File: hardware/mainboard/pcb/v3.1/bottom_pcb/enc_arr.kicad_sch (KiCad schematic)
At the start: 24 parts

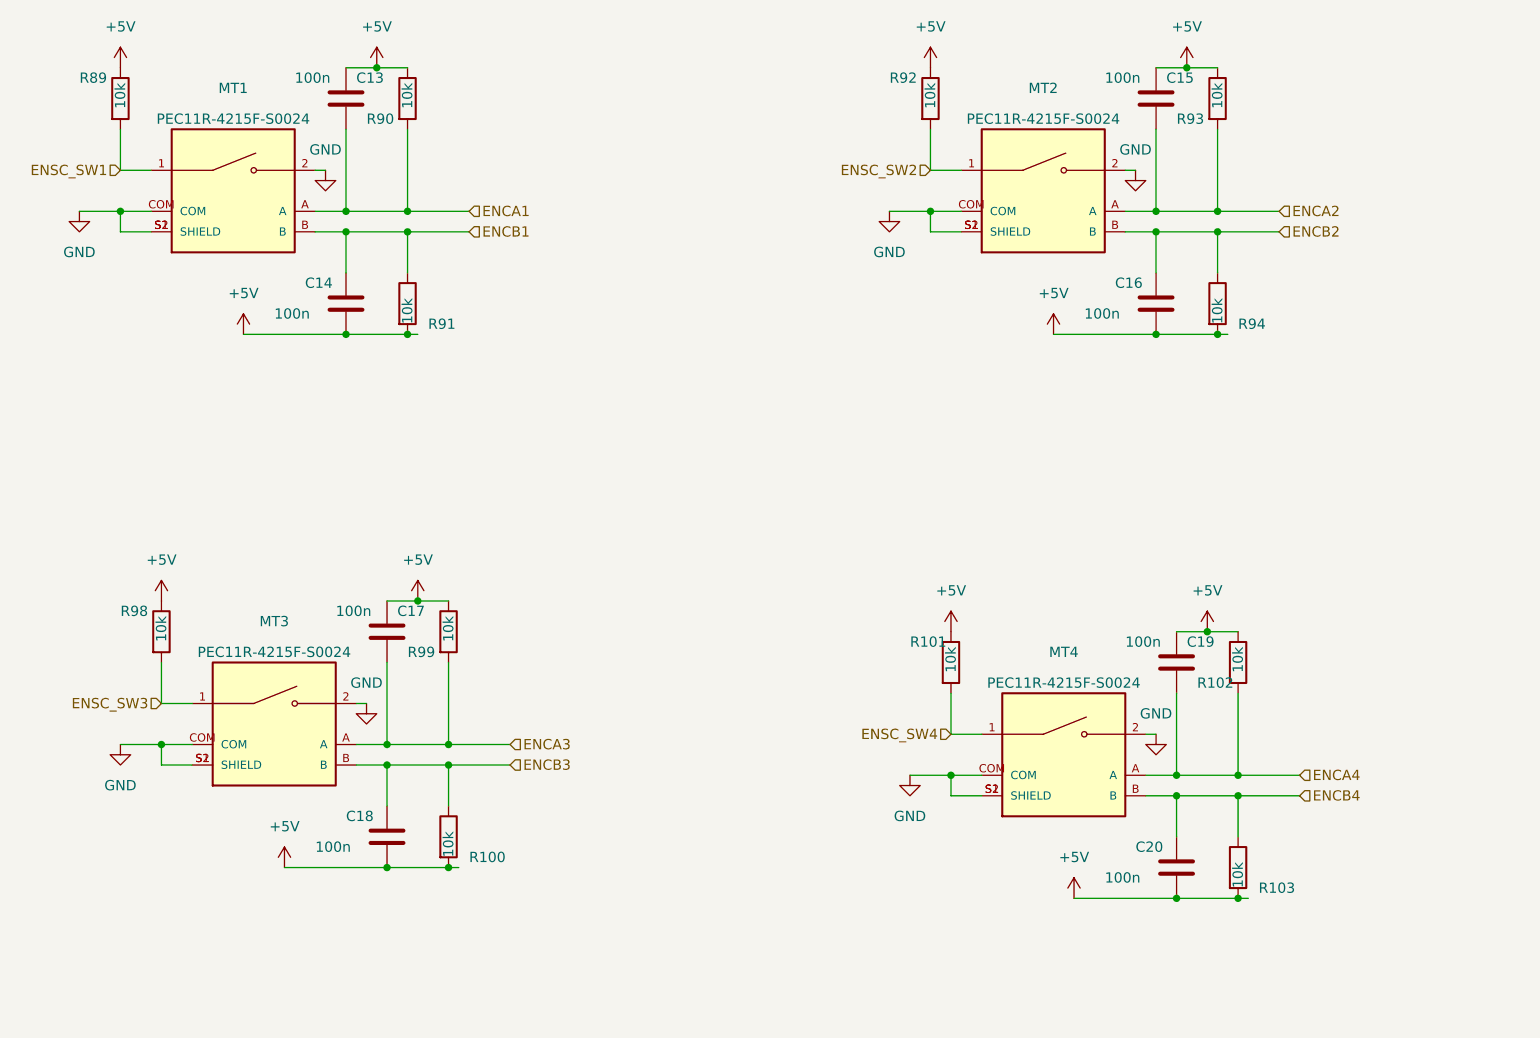
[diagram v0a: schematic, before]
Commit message: pcb cut off
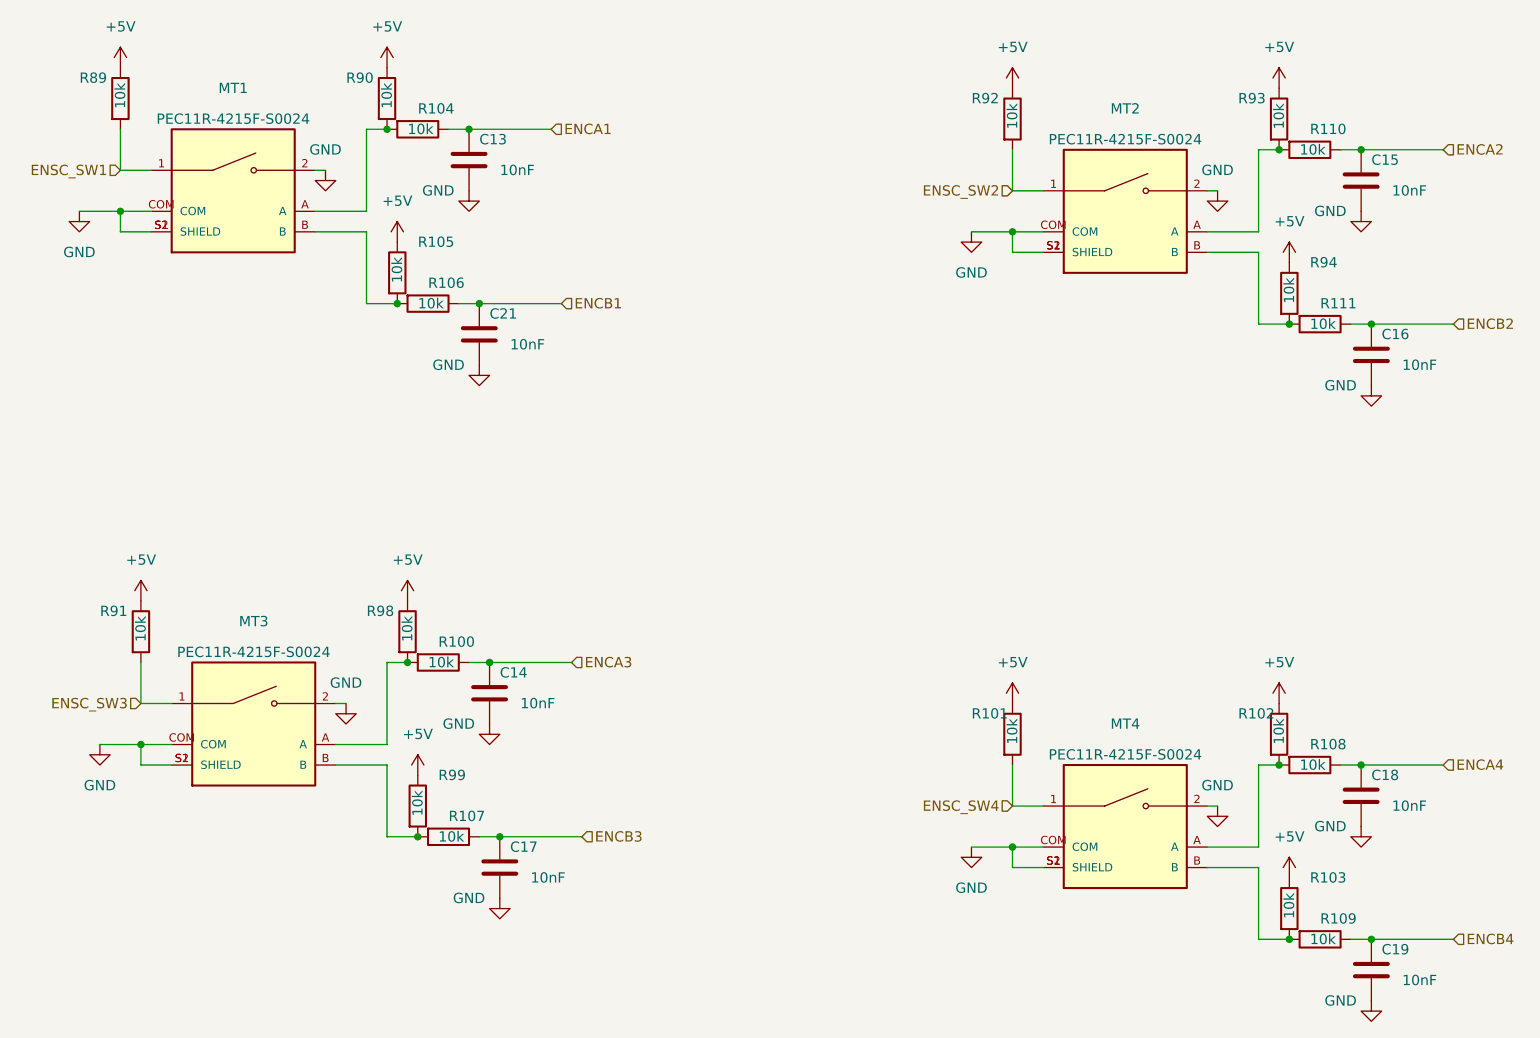
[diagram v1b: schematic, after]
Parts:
- removed C20: 100n, Capacitor_SMD:C_1206_3216Metric_Pad1.33x1.80mm_HandSolder, symbol Device:C
- added C21: 10nF, Capacitor_SMD:C_1206_3216Metric_Pad1.33x1.80mm_HandSolder, symbol Device:C
- added R104, R105, R106, R107, R108, R109, R110, R111: 10k, Resistor_SMD:R_1206_3216Metric_Pad1.30x1.75mm_HandSolder, symbol Device:R
- C13, C14, C15, C16, C17, C18, C19: value 100n -> 10nF
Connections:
- net +5V: now also R103.1, R91.1, R94.1, R105.1; no longer C13.1, C14.2, C15.1, C16.2, C17.1, C18.2, C19.1, R100.2, R103.2, R91.2, R94.2
- net ENCA1: now also C13.1, R104.1; no longer C13.2, MT1.A, R90.2
- net ENCA2: now also C15.1, R110.1; no longer C15.2, MT2.A, R93.2
- net ENCA3: now also C14.1, R100.1; no longer C17.2, MT3.A, R99.2
- net ENCA4: now also C18.1, R108.1; no longer C19.2, MT4.A, R102.2
- net ENCB1: now also C21.1, R106.1; no longer C14.1, MT1.B, R91.1
- net ENCB2: now also R111.1; no longer MT2.B, R94.1
- net ENCB3: now also C17.1, R107.1; no longer C18.1, MT3.B, R100.1
- net ENCB4: now also C19.1, R109.1; no longer MT4.B, R103.1
- net ENSC_SW3: now also R91.2; no longer R98.2
- net GND: now also C13.2, C14.2, C15.2, C16.2, C17.2, C18.2, C19.2, C21.2
- new net: MT1.A, R104.2, R90.2
- new net: MT1.B, R105.2, R106.2
- new net: MT2.B, R111.2, R94.2
- new net: MT4.A, R102.2, R108.2
- new net: MT4.B, R103.2, R109.2
- new net: MT3.A, R100.2, R98.2
- new net: MT2.A, R110.2, R93.2
- new net: MT3.B, R107.2, R99.2
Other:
- moved on the sheet: C13, MT2, MT3, MT4, R90
